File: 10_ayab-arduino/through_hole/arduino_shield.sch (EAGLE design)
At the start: 23 parts, among them IC3 MCP2300X/P, IC4 MCP2300X/P, X1 NEB1R

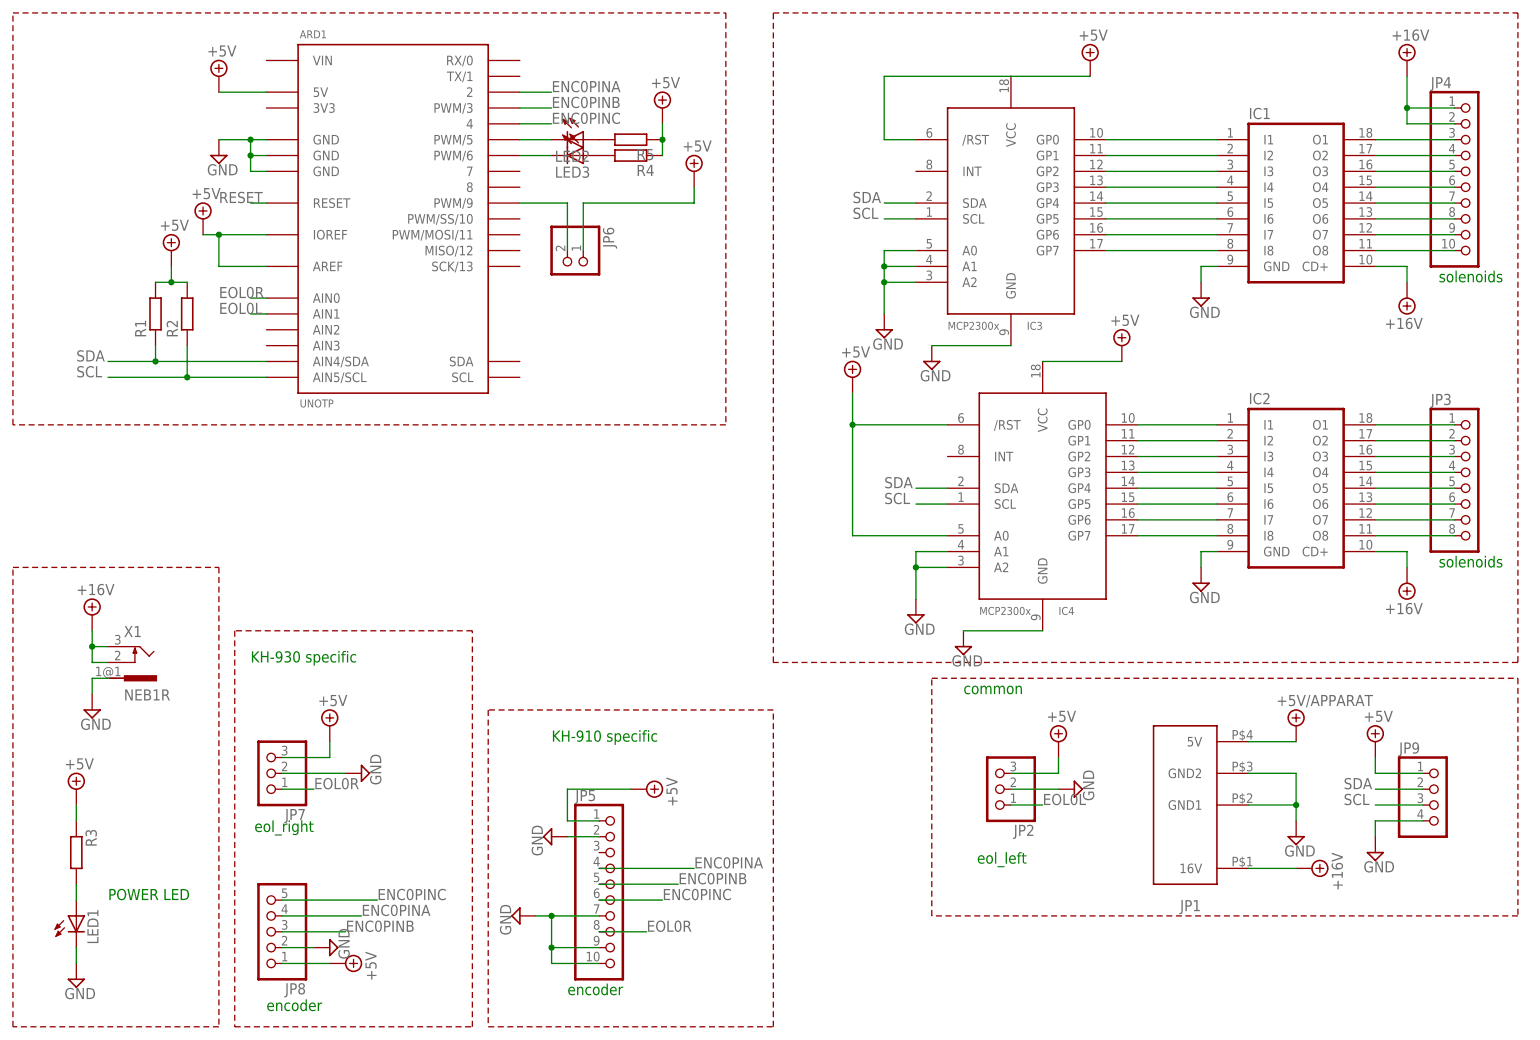
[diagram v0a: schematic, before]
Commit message: /andz added 2mm holes for other machine types
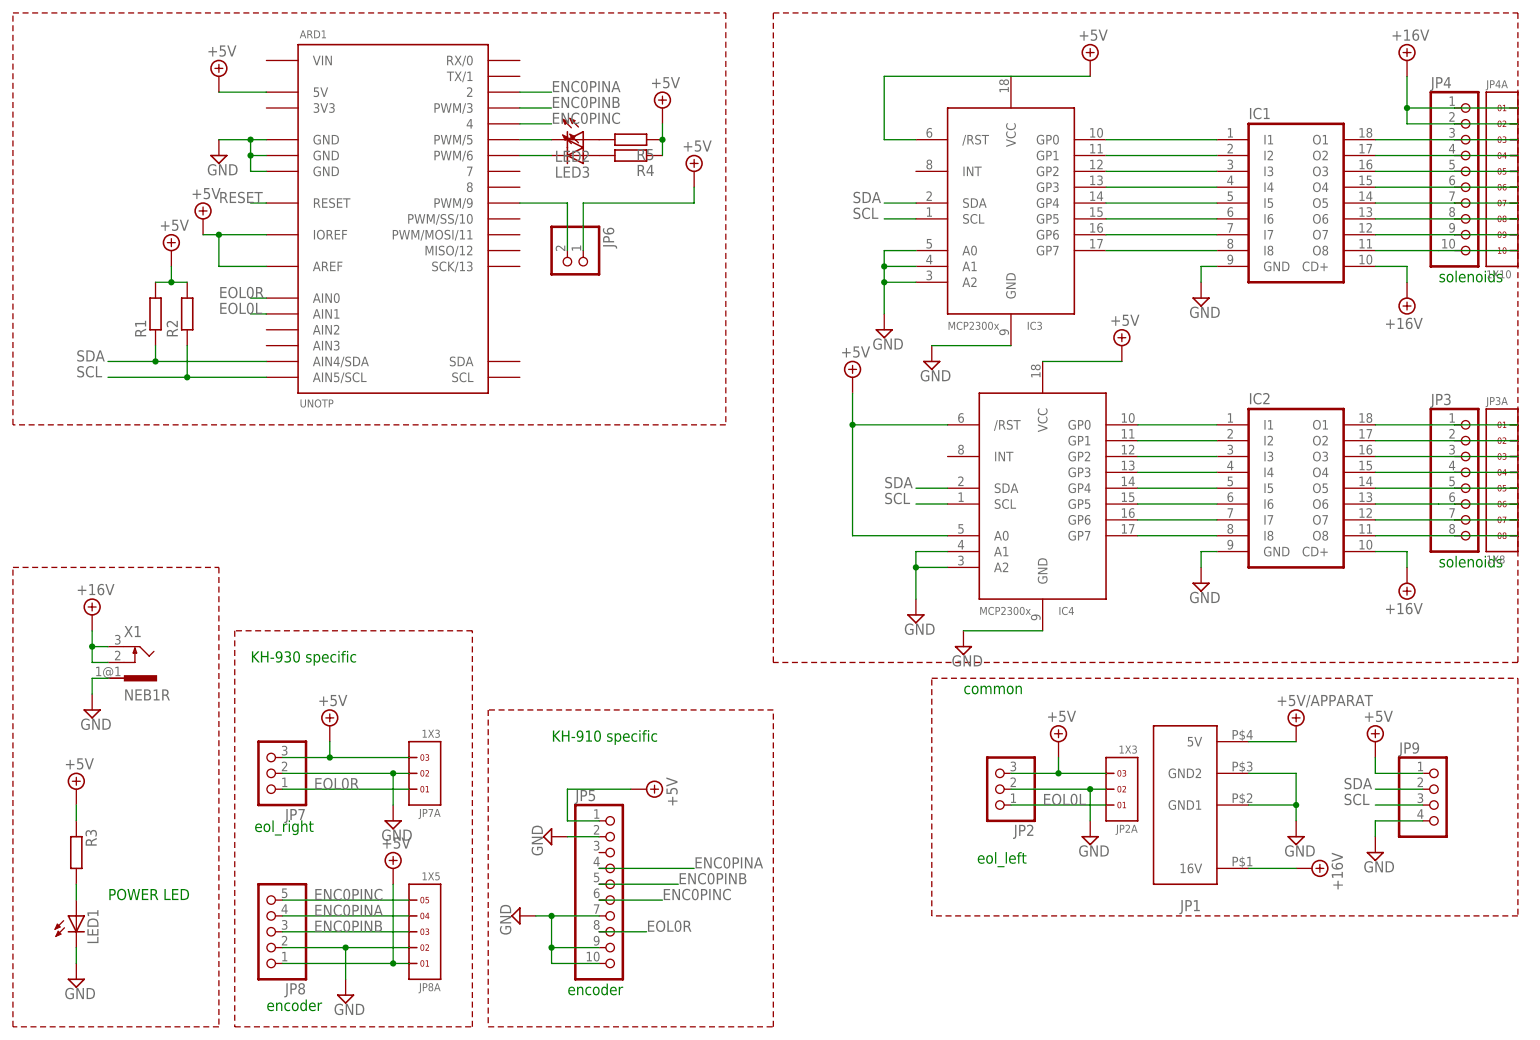
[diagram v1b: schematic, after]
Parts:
- added JP2A, JP7A: 1X3, headers_2mm:1X3
- added JP3A: 1X8, headers_2mm:1X8
- added JP4A: 1X10, headers_2mm:1X10
- added JP8A: 1X5, headers_2mm:1X5
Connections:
- net +15V: now also JP4A.1, JP4A.2
- net +5V: now also JP2A.3, JP7A.3, JP8A.1
- net ENC0PINA: now also JP8A.4
- net ENC0PINB: now also JP8A.3
- net ENC0PINC: now also JP8A.5
- net EOL0L: now also JP2A.1
- net EOL0R: now also JP7A.1
- net GND: now also JP2A.2, JP7A.2, JP8A.2
- net N$17: now also JP3A.1
- net N$18: now also JP3A.2
- net N$19: now also JP3A.3
- net N$20: now also JP3A.4
- net N$21: now also JP3A.5
- net N$22: now also JP3A.6
- net N$23: now also JP3A.7
- net N$24: now also JP3A.8
- net N$25: now also JP4A.10
- net N$26: now also JP4A.9
- net N$27: now also JP4A.8
- net N$28: now also JP4A.7
- net N$29: now also JP4A.6
- net N$30: now also JP4A.5
- net N$31: now also JP4A.4
- net N$32: now also JP4A.3
